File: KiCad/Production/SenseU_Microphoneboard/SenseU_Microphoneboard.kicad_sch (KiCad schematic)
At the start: 12 parts, among them J1 90122-0126, U1 SPH0645LM4H-B, U2 SPH0645LM4H-B, U3 SPH0645LM4H-B

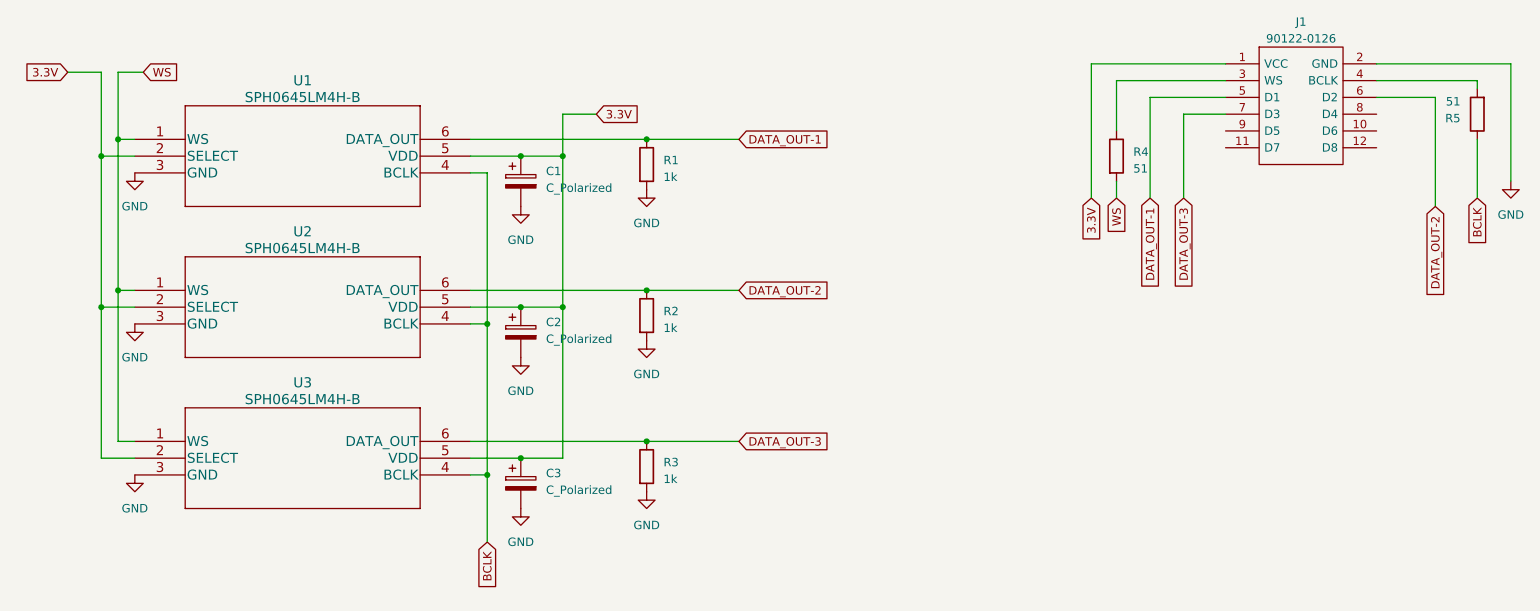
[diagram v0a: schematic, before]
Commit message: PCB design V1 without routing or component placement
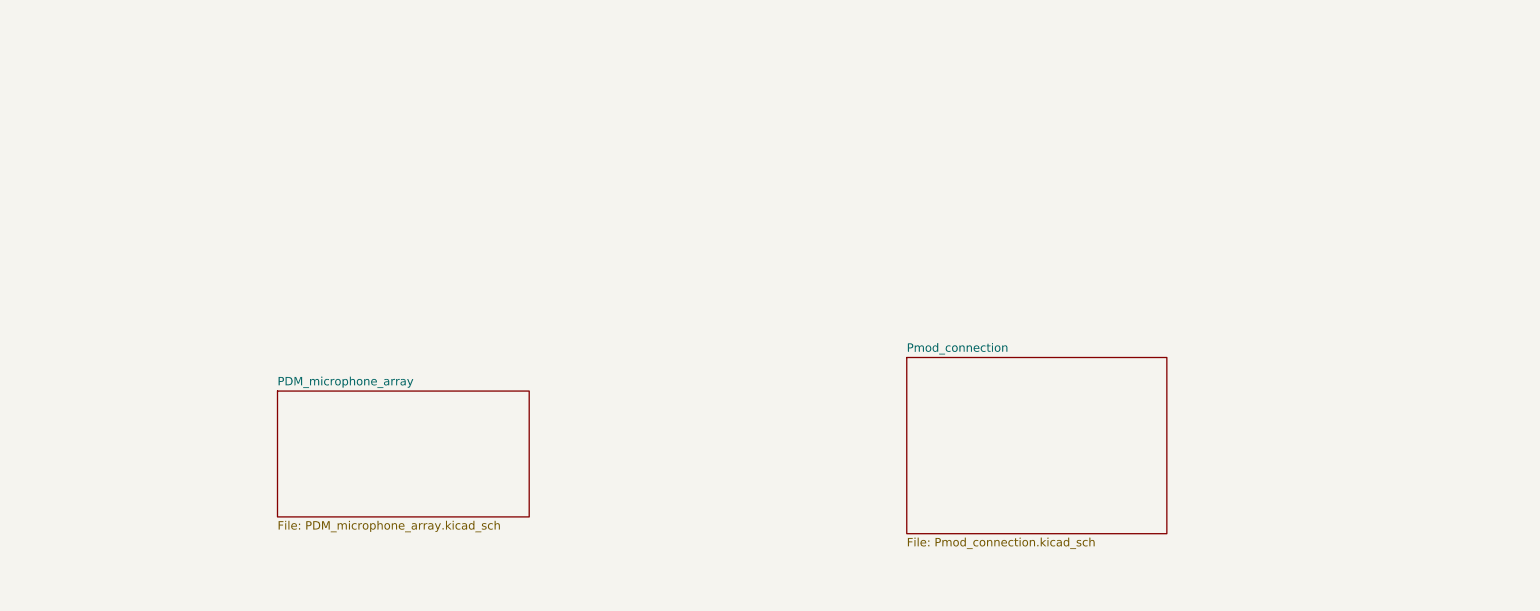
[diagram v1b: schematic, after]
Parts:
- removed C1, C2, C3: C_Polarized, Capacitor_SMD:CP_Elec_3x5.3, symbol Device:C_Polarized
- removed J1: 90122-0126, HDRRA12W65P254_2X6_1516X250X615P, symbol SensU_Microphone_parts:90122-0126
- removed R1, R2, R3: 1k, Resistor_SMD:R_0603_1608Metric_Pad0.98x0.95mm_HandSolder, symbol Device:R
- removed R4, R5: 51, Resistor_SMD:R_0603_1608Metric_Pad0.98x0.95mm_HandSolder, symbol Device:R
- removed U1, U2, U3: SPH0645LM4H-B, SPH0645LM4H-B_KNO, symbol SensU_Microphone_parts:SPH0645LM4H-B
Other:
- added sheet PDM_microphone_array (PDM_microphone_array.kicad_sch)
- added sheet Pmod_connection (Pmod_connection.kicad_sch)
